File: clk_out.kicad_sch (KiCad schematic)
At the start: 14 parts

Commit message: Schematic updated
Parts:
- C701, C702, C703: renamed from C?; footprint (none) -> Capacitor_SMD:C_0805_2012Metric
- R701, R702: renamed from R?; footprint (none) -> Resistor_SMD:R_0805_2012Metric
- gave numbers to parts that had none: 6
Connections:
- net +3.3VA renamed +3.3VD
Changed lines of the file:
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@@
   (symbol (lib_id "symbols:74LVC1G157") (at 139.7 57.15 0) (unit 2)
     (in_bom yes) (on_board yes) (fields_autoplaced)
-    (property "Reference" "U?" (id 0) (at 137.4787 56.2415 0)
+    (property "Reference" "U701" (id 0) (at 137.4787 56.2415 0)
       (effects (font (size 1.27 1.27)) (justify right))
     )
@@
   (symbol (lib_id "Device:R") (at 184.15 101.6 270) (unit 1)
     (in_bom yes) (on_board yes) (fields_autoplaced)
-    (property "Reference" "R?" (id 0) (at 184.15 96.6175 90))
+    (property "Reference" "R701" (id 0) (at 184.15 96.6175 90))
     (property "Value" "75" (id 1) (at 184.15 99.3926 90))
-    (property "Footprint" "" (id 2) (at 184.15 99.822 90)
+    (property "Footprint" "Resistor_SMD:R_0805_2012Metric" (id 2) (at 184.15 99.822 90)
       (effects (font (size 1.27 1.27)) hide)
     )
@@
   (symbol (lib_id "power:GND") (at 190.5 113.03 0) (unit 1)
     (in_bom yes) (on_board yes) (fields_autoplaced)
-    (property "Reference" "#PWR?" (id 0) (at 190.5 119.38 0)
+    (property "Reference" "#PWR0705" (id 0) (at 190.5 119.38 0)
       (effects (font (size 1.27 1.27)) hide)
     )
@@
   (symbol (lib_id "Device:C") (at 171.45 101.6 90) (unit 1)
     (in_bom yes) (on_board yes) (fields_autoplaced)
-    (property "Reference" "C?" (id 0) (at 171.45 95.4745 90))
+    (property "Reference" "C702" (id 0) (at 171.45 95.4745 90))
     (property "Value" "100n" (id 1) (at 171.45 98.2496 90))
-    (property "Footprint" "" (id 2) (at 175.26 100.6348 0)
+    (property "Footprint" "Capacitor_SMD:C_0805_2012Metric" (id 2) (at 175.26 100.6348 0)
       (effects (font (size 1.27 1.27)) hide)
     )
@@
     (pin "2")
   )
-  (symbol (lib_id "symbols:+3.3VD") (at 152.4 90.17 0) (unit 1)
-    (in_bom yes) (on_board yes) (fields_autoplaced)
-    (property "Reference" "#PWR?" (id 0) (at 152.4 93.98 0)
+  (symbol (lib_name "+3.3VD_1") (lib_id "symbols:+3.3VD") (at 152.4 90.17 0) (unit 1)
+    (in_bom yes) (on_board yes) (fields_autoplaced)
+    (property "Reference" "#PWR0703" (id 0) (at 152.4 93.98 0)
       (effects (font (size 1.27 1.27)) hide)
     )
@@
   (symbol (lib_id "symbols:74LVC2G04") (at 128.27 93.98 0) (unit 1)
     (in_bom yes) (on_board yes)
-    (property "Reference" "U?" (id 0) (at 130.1115 84.9335 0))
+    (property "Reference" "U702" (id 0) (at 130.1115 84.9335 0))
     (property "Value" "74LVC2G04" (id 1) (at 130.1115 87.7086 0))
     (property "Footprint" "Package_TO_SOT_SMD:SOT-23-6" (id 2) (at 128.27 76.2 0)
@@
   (symbol (lib_id "Diode:BAT54J") (at 152.4 107.95 270) (unit 1)
     (in_bom yes) (on_board yes) (fields_autoplaced)
-    (property "Reference" "D?" (id 0) (at 154.432 106.724 90)
+    (property "Reference" "D702" (id 0) (at 154.432 106.724 90)
       (effects (font (size 1.27 1.27)) (justify left))
     )
@@
   (symbol (lib_id "Jumper:Jumper_2_Open") (at 171.45 90.17 0) (unit 1)
     (in_bom yes) (on_board yes) (fields_autoplaced)
-    (property "Reference" "JP?" (id 0) (at 171.45 84.5525 0))
+    (property "Reference" "JP701" (id 0) (at 171.45 84.5525 0))
     (property "Value" "DC" (id 1) (at 171.45 87.3276 0))
     (property "Footprint" "" (id 2) (at 171.45 90.17 0)
@@
   (symbol (lib_id "Device:R") (at 190.5 107.95 180) (unit 1)
     (in_bom yes) (on_board yes) (fields_autoplaced)
-    (property "Reference" "R?" (id 0) (at 188.722 107.0415 0)
+    (property "Reference" "R702" (id 0) (at 188.722 107.0415 0)
       (effects (font (size 1.27 1.27)) (justify left))
     )
@@
       (effects (font (size 1.27 1.27)) (justify left))
     )
-    (property "Footprint" "" (id 2) (at 192.278 107.95 90)
+    (property "Footprint" "Resistor_SMD:R_0805_2012Metric" (id 2) (at 192.278 107.95 90)
       (effects (font (size 1.27 1.27)) hide)
     )
@@
   (symbol (lib_id "power:GND") (at 152.4 113.03 0) (unit 1)
     (in_bom yes) (on_board yes) (fields_autoplaced)
-    (property "Reference" "#PWR?" (id 0) (at 152.4 119.38 0)
+    (property "Reference" "#PWR0704" (id 0) (at 152.4 119.38 0)
       (effects (font (size 1.27 1.27)) hide)
     )
@@
   (symbol (lib_id "symbols:+3.3VD") (at 139.7 50.8 0) (unit 1)
     (in_bom yes) (on_board yes) (fields_autoplaced)
-    (property "Reference" "#PWR?" (id 0) (at 139.7 54.61 0)
+    (property "Reference" "#PWR0701" (id 0) (at 139.7 54.61 0)
       (effects (font (size 1.27 1.27)) hide)
     )
@@
   (symbol (lib_id "power:GND") (at 139.7 63.5 0) (unit 1)
     (in_bom yes) (on_board yes) (fields_autoplaced)
-    (property "Reference" "#PWR?" (id 0) (at 139.7 69.85 0)
+    (property "Reference" "#PWR0702" (id 0) (at 139.7 69.85 0)
       (effects (font (size 1.27 1.27)) hide)
     )
@@
   (symbol (lib_id "power:GND") (at 203.2 113.03 0) (unit 1)
     (in_bom yes) (on_board yes) (fields_autoplaced)
-    (property "Reference" "#PWR?" (id 0) (at 203.2 119.38 0)
+    (property "Reference" "#PWR0706" (id 0) (at 203.2 119.38 0)
       (effects (font (size 1.27 1.27)) hide)
     )
@@
   (symbol (lib_id "Diode:BAT54J") (at 152.4 95.25 270) (unit 1)
     (in_bom yes) (on_board yes) (fields_autoplaced)
-    (property "Reference" "D?" (id 0) (at 154.432 94.024 90)
+    (property "Reference" "D701" (id 0) (at 154.432 94.024 90)
       (effects (font (size 1.27 1.27)) (justify left))
     )
@@
   (symbol (lib_id "Device:C") (at 177.8 57.15 180) (unit 1)
     (in_bom yes) (on_board yes) (fields_autoplaced)
-    (property "Reference" "C?" (id 0) (at 180.721 56.2415 0)
+    (property "Reference" "C703" (id 0) (at 180.721 56.2415 0)
       (effects (font (size 1.27 1.27)) (justify right))
     )
@@
       (effects (font (size 1.27 1.27)) (justify right))
     )
-    (property "Footprint" "" (id 2) (at 176.8348 53.34 0)
+    (property "Footprint" "Capacitor_SMD:C_0805_2012Metric" (id 2) (at 176.8348 53.34 0)
       (effects (font (size 1.27 1.27)) hide)
     )
@@
   (symbol (lib_id "Device:D_TVS") (at 203.2 107.95 90) (unit 1)
     (in_bom yes) (on_board yes) (fields_autoplaced)
-    (property "Reference" "D?" (id 0) (at 201.1681 107.0415 90)
+    (property "Reference" "D703" (id 0) (at 201.1681 107.0415 90)
       (effects (font (size 1.27 1.27)) (justify left))
     )
@@
   (symbol (lib_id "symbols:74LVC2G04") (at 152.4 57.15 0) (unit 3)
     (in_bom yes) (on_board yes)
-    (property "Reference" "U?" (id 0) (at 151.13 48.26 0)
+    (property "Reference" "U702" (id 0) (at 151.13 48.26 0)
       (effects (font (size 1.27 1.27)) (justify left))
     )
@@
     (pin "5")
   )
-  (symbol (lib_name "74LVC1G157_1") (lib_id "symbols:74LVC1G157") (at 104.14 101.6 0) (unit 1)
-    (in_bom yes) (on_board yes) (fields_autoplaced)
-    (property "Reference" "U?" (id 0) (at 104.14 90.7755 0))
+  (symbol (lib_id "symbols:74LVC1G157") (at 104.14 101.6 0) (unit 1)
+    (in_bom yes) (on_board yes) (fields_autoplaced)
+    (property "Reference" "U701" (id 0) (at 104.14 90.7755 0))
     (property "Value" "74LVC1G157" (id 1) (at 104.14 93.5506 0))
     (property "Footprint" "Package_TO_SOT_SMD:SOT-23-6" (id 2) (at 104.14 92.075 0)
@@
   (symbol (lib_id "Device:C") (at 165.1 57.15 180) (unit 1)
     (in_bom yes) (on_board yes) (fields_autoplaced)
-    (property "Reference" "C?" (id 0) (at 168.021 56.2415 0)
+    (property "Reference" "C701" (id 0) (at 168.021 56.2415 0)
       (effects (font (size 1.27 1.27)) (justify right))
     )
@@
       (effects (font (size 1.27 1.27)) (justify right))
     )
-    (property "Footprint" "" (id 2) (at 164.1348 53.34 0)
+    (property "Footprint" "Capacitor_SMD:C_0805_2012Metric" (id 2) (at 164.1348 53.34 0)
       (effects (font (size 1.27 1.27)) hide)
     )
@@
   (symbol (lib_id "symbols:74LVC2G04") (at 128.27 109.22 0) (unit 2)
     (in_bom yes) (on_board yes) (fields_autoplaced)
-    (property "Reference" "U?" (id 0) (at 130.1115 101.4435 0))
+    (property "Reference" "U702" (id 0) (at 130.1115 101.4435 0))
     (property "Value" "74LVC2G04" (id 1) (at 130.1115 104.2186 0))
     (property "Footprint" "Package_TO_SOT_SMD:SOT-23-6" (id 2) (at 128.27 91.44 0)

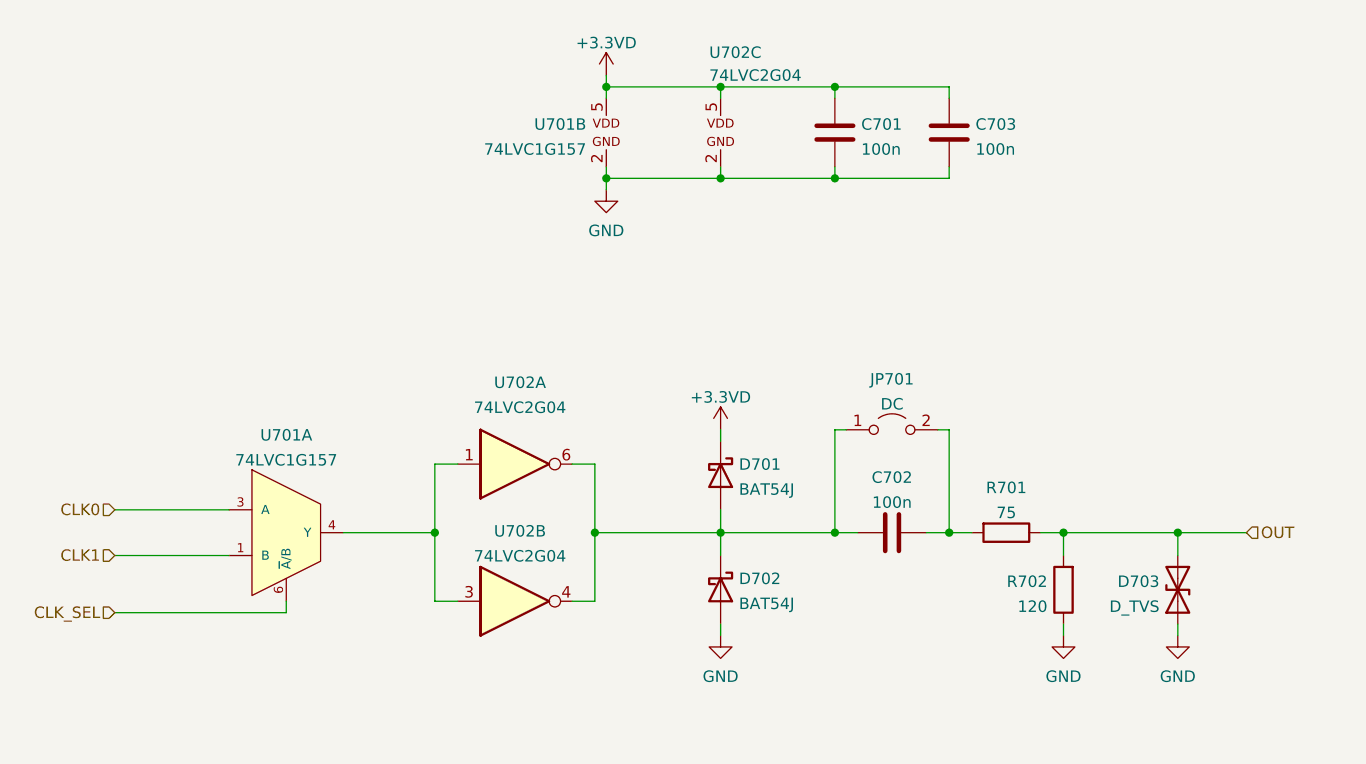
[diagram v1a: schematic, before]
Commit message: Schematic sketching done
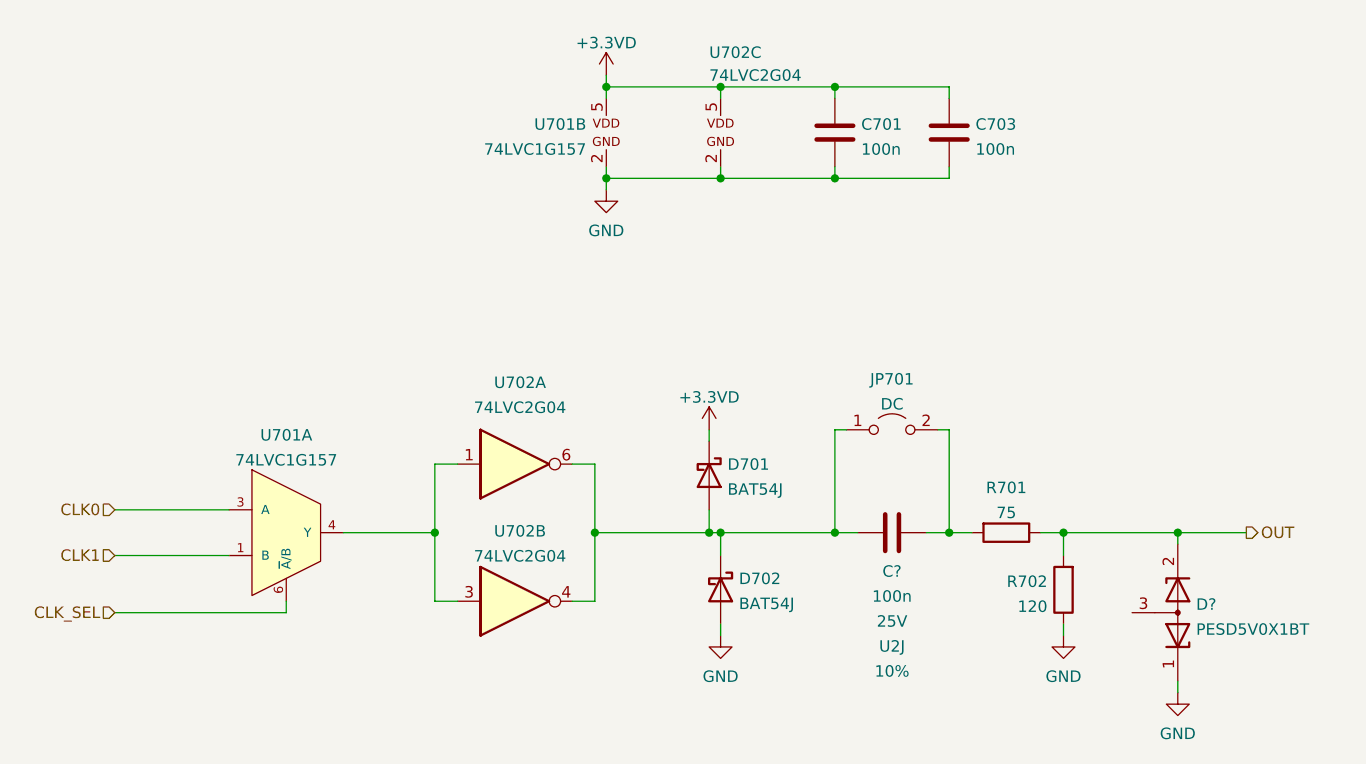
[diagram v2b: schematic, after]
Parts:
- removed C702: 100n, Capacitor_SMD:C_0805_2012Metric, symbol Device:C
- removed D703: D_TVS, symbol Device:D_TVS
- added C?: 100n, Capacitor_SMD:C_0805_2012Metric, symbol Device:C
- added D?: PESD5V0X1BT, Package_TO_SOT_SMD:SOT-23, symbol Device:D_Zener_Dual_CommonAnode_KKA
- R701, R702: Tolerance (none) -> 5%
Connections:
- net GND: now also D?.1 (K)
- net OUT: now also D?.2 (K)
- net at JP701.2 (B), R701.2: now also C?.2
- net at D701.2 (A), D702.1 (K), JP701.1 (A)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: now also C?.1
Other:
- moved on the sheet: D701

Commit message: Update schematic layout, separate into sheets
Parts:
- gave numbers to parts that had none: 2
- renumbered C701 to C1001, C703 to C1003, D701 to D1001, D702 to D1002, JP701 to JP1001, R701 to R1001, R702 to R1002, U701 to U1001, U702 to U1002
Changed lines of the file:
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@@
   (symbol (lib_id "symbols:74LVC1G157") (at 139.7 57.15 0) (unit 2)
     (in_bom yes) (on_board yes) (fields_autoplaced)
-    (property "Reference" "U701" (id 0) (at 137.4787 56.2415 0)
+    (property "Reference" "U1001" (id 0) (at 137.4787 56.2415 0)
       (effects (font (size 1.27 1.27)) (justify right))
     )
@@
   (symbol (lib_id "Device:R") (at 184.15 101.6 270) (unit 1)
     (in_bom yes) (on_board yes) (fields_autoplaced)
-    (property "Reference" "R701" (id 0) (at 184.15 96.6175 90))
+    (property "Reference" "R1001" (id 0) (at 184.15 96.6175 90))
     (property "Value" "75" (id 1) (at 184.15 99.3926 90))
     (property "Footprint" "Resistor_SMD:R_0805_2012Metric" (id 2) (at 184.15 99.822 90)
@@
   (symbol (lib_id "power:GND") (at 203.2 119.38 0) (unit 1)
     (in_bom yes) (on_board yes) (fields_autoplaced)
-    (property "Reference" "#PWR?" (id 0) (at 203.2 125.73 0)
+    (property "Reference" "#PWR01006" (id 0) (at 203.2 125.73 0)
       (effects (font (size 1.27 1.27)) hide)
     )
@@
   (symbol (lib_id "power:GND") (at 190.5 113.03 0) (unit 1)
     (in_bom yes) (on_board yes) (fields_autoplaced)
-    (property "Reference" "#PWR0705" (id 0) (at 190.5 119.38 0)
+    (property "Reference" "#PWR01005" (id 0) (at 190.5 119.38 0)
       (effects (font (size 1.27 1.27)) hide)
     )
@@
   (symbol (lib_id "Device:C") (at 171.45 101.6 90) (unit 1)
     (in_bom yes) (on_board yes) (fields_autoplaced)
-    (property "Reference" "C?" (id 0) (at 171.45 105.9085 90))
+    (property "Reference" "C1002" (id 0) (at 171.45 105.9085 90))
     (property "Value" "100n" (id 1) (at 171.45 108.6836 90))
     (property "Footprint" "Capacitor_SMD:C_0805_2012Metric" (id 2) (at 175.26 100.6348 0)
@@
     (pin "2")
   )
-  (symbol (lib_name "+3.3VD_1") (lib_id "symbols:+3.3VD") (at 151.13 90.17 0) (unit 1)
-    (in_bom yes) (on_board yes) (fields_autoplaced)
-    (property "Reference" "#PWR0703" (id 0) (at 151.13 93.98 0)
+  (symbol (lib_id "symbols:+3.3VD") (at 151.13 90.17 0) (unit 1)
+    (in_bom yes) (on_board yes) (fields_autoplaced)
+    (property "Reference" "#PWR01003" (id 0) (at 151.13 93.98 0)
       (effects (font (size 1.27 1.27)) hide)
     )
@@
   (symbol (lib_id "symbols:74LVC2G04") (at 128.27 93.98 0) (unit 1)
     (in_bom yes) (on_board yes)
-    (property "Reference" "U702" (id 0) (at 130.1115 84.9335 0))
+    (property "Reference" "U1002" (id 0) (at 130.1115 84.9335 0))
     (property "Value" "74LVC2G04" (id 1) (at 130.1115 87.7086 0))
     (property "Footprint" "Package_TO_SOT_SMD:SOT-23-6" (id 2) (at 128.27 76.2 0)
@@
   (symbol (lib_id "Diode:BAT54J") (at 152.4 107.95 270) (unit 1)
     (in_bom yes) (on_board yes) (fields_autoplaced)
-    (property "Reference" "D702" (id 0) (at 154.432 106.724 90)
+    (property "Reference" "D1002" (id 0) (at 154.432 106.724 90)
       (effects (font (size 1.27 1.27)) (justify left))
     )
@@
   (symbol (lib_id "Device:D_Zener_Dual_CommonAnode_KKA") (at 203.2 110.49 270) (mirror x) (unit 1)
     (in_bom yes) (on_board yes) (fields_autoplaced)
-    (property "Reference" "D?" (id 0) (at 205.232 109.5815 90)
+    (property "Reference" "D1003" (id 0) (at 205.232 109.5815 90)
       (effects (font (size 1.27 1.27)) (justify left))
     )
@@
   (symbol (lib_id "Jumper:Jumper_2_Open") (at 171.45 90.17 0) (unit 1)
     (in_bom yes) (on_board yes) (fields_autoplaced)
-    (property "Reference" "JP701" (id 0) (at 171.45 84.5525 0))
+    (property "Reference" "JP1001" (id 0) (at 171.45 84.5525 0))
     (property "Value" "DC" (id 1) (at 171.45 87.3276 0))
     (property "Footprint" "" (id 2) (at 171.45 90.17 0)
@@
   (symbol (lib_id "Device:R") (at 190.5 107.95 180) (unit 1)
     (in_bom yes) (on_board yes) (fields_autoplaced)
-    (property "Reference" "R702" (id 0) (at 188.722 107.0415 0)
+    (property "Reference" "R1002" (id 0) (at 188.722 107.0415 0)
       (effects (font (size 1.27 1.27)) (justify left))
     )
@@
   (symbol (lib_id "power:GND") (at 152.4 113.03 0) (unit 1)
     (in_bom yes) (on_board yes) (fields_autoplaced)
-    (property "Reference" "#PWR0704" (id 0) (at 152.4 119.38 0)
+    (property "Reference" "#PWR01004" (id 0) (at 152.4 119.38 0)
       (effects (font (size 1.27 1.27)) hide)
     )
@@
   (symbol (lib_id "symbols:+3.3VD") (at 139.7 50.8 0) (unit 1)
     (in_bom yes) (on_board yes) (fields_autoplaced)
-    (property "Reference" "#PWR0701" (id 0) (at 139.7 54.61 0)
+    (property "Reference" "#PWR01001" (id 0) (at 139.7 54.61 0)
       (effects (font (size 1.27 1.27)) hide)
     )
@@
   (symbol (lib_id "power:GND") (at 139.7 63.5 0) (unit 1)
     (in_bom yes) (on_board yes) (fields_autoplaced)
-    (property "Reference" "#PWR0702" (id 0) (at 139.7 69.85 0)
+    (property "Reference" "#PWR01002" (id 0) (at 139.7 69.85 0)
       (effects (font (size 1.27 1.27)) hide)
     )
@@
   (symbol (lib_id "Diode:BAT54J") (at 151.13 95.25 270) (unit 1)
     (in_bom yes) (on_board yes) (fields_autoplaced)
-    (property "Reference" "D701" (id 0) (at 153.162 94.024 90)
+    (property "Reference" "D1001" (id 0) (at 153.162 94.024 90)
       (effects (font (size 1.27 1.27)) (justify left))
     )
@@
   (symbol (lib_id "Device:C") (at 177.8 57.15 180) (unit 1)
     (in_bom yes) (on_board yes) (fields_autoplaced)
-    (property "Reference" "C703" (id 0) (at 180.721 56.2415 0)
+    (property "Reference" "C1003" (id 0) (at 180.721 56.2415 0)
       (effects (font (size 1.27 1.27)) (justify right))
     )
@@
   (symbol (lib_id "symbols:74LVC2G04") (at 152.4 57.15 0) (unit 3)
     (in_bom yes) (on_board yes)
-    (property "Reference" "U702" (id 0) (at 151.13 48.26 0)
+    (property "Reference" "U1002" (id 0) (at 151.13 48.26 0)
       (effects (font (size 1.27 1.27)) (justify left))
     )
@@
   (symbol (lib_id "symbols:74LVC1G157") (at 104.14 101.6 0) (unit 1)
     (in_bom yes) (on_board yes) (fields_autoplaced)
-    (property "Reference" "U701" (id 0) (at 104.14 90.7755 0))
+    (property "Reference" "U1001" (id 0) (at 104.14 90.7755 0))
     (property "Value" "74LVC1G157" (id 1) (at 104.14 93.5506 0))
     (property "Footprint" "Package_TO_SOT_SMD:SOT-23-6" (id 2) (at 104.14 92.075 0)
@@
   (symbol (lib_id "Device:C") (at 165.1 57.15 180) (unit 1)
     (in_bom yes) (on_board yes) (fields_autoplaced)
-    (property "Reference" "C701" (id 0) (at 168.021 56.2415 0)
+    (property "Reference" "C1001" (id 0) (at 168.021 56.2415 0)
       (effects (font (size 1.27 1.27)) (justify right))
     )
@@
   (symbol (lib_id "symbols:74LVC2G04") (at 128.27 109.22 0) (unit 2)
     (in_bom yes) (on_board yes) (fields_autoplaced)
-    (property "Reference" "U702" (id 0) (at 130.1115 101.4435 0))
+    (property "Reference" "U1002" (id 0) (at 130.1115 101.4435 0))
     (property "Value" "74LVC2G04" (id 1) (at 130.1115 104.2186 0))
     (property "Footprint" "Package_TO_SOT_SMD:SOT-23-6" (id 2) (at 128.27 91.44 0)

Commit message: Schematic update
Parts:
- C1001: value 100n -> 1u; Spec1 (none) -> 16V; Spec2 (none) -> X5R; Tolerance (none) -> 20%
- C1002: footprint Capacitor_SMD:C_0805_2012Metric -> Capacitor_SMD:C_1206_3216Metric
- C1003: Spec1 (none) -> 16V; Spec2 (none) -> X5R; Tolerance (none) -> 20%
- JP1001: footprint (none) -> Connector_PinHeader_2.54mm:PinHeader_1x02_P2.54mm_Vertical
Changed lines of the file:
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@@
     (property "Reference" "C1002" (id 0) (at 171.45 105.9085 90))
     (property "Value" "100n" (id 1) (at 171.45 108.6836 90))
-    (property "Footprint" "Capacitor_SMD:C_0805_2012Metric" (id 2) (at 175.26 100.6348 0)
+    (property "Footprint" "Capacitor_SMD:C_1206_3216Metric" (id 2) (at 175.26 100.6348 0)
       (effects (font (size 1.27 1.27)) hide)
     )
@@
     (property "Reference" "JP1001" (id 0) (at 171.45 84.5525 0))
     (property "Value" "DC" (id 1) (at 171.45 87.3276 0))
-    (property "Footprint" "" (id 2) (at 171.45 90.17 0)
+    (property "Footprint" "Connector_PinHeader_2.54mm:PinHeader_1x02_P2.54mm_Vertical" (id 2) (at 171.45 90.17 0)
       (effects (font (size 1.27 1.27)) hide)
     )
@@
     )
     (property "Datasheet" "~" (id 3) (at 177.8 57.15 0)
+      (effects (font (size 1.27 1.27)) hide)
+    )
+    (property "Spec1" "16V" (id 4) (at 177.8 57.15 0)
+      (effects (font (size 1.27 1.27)) hide)
+    )
+    (property "Spec2" "X5R" (id 5) (at 177.8 57.15 0)
+      (effects (font (size 1.27 1.27)) hide)
+    )
+    (property "Tolerance" "20%" (id 6) (at 177.8 57.15 0)
       (effects (font (size 1.27 1.27)) hide)
     )
@@
       (effects (font (size 1.27 1.27)) (justify right))
     )
-    (property "Value" "100n" (id 1) (at 168.021 59.0166 0)
+    (property "Value" "1u" (id 1) (at 168.021 59.0166 0)
       (effects (font (size 1.27 1.27)) (justify right))
     )
@@
       (effects (font (size 1.27 1.27)) hide)
     )
+    (property "Spec1" "16V" (id 4) (at 165.1 57.15 0)
+      (effects (font (size 1.27 1.27)) hide)
+    )
+    (property "Spec2" "X5R" (id 5) (at 165.1 57.15 0)
+      (effects (font (size 1.27 1.27)) hide)
+    )
+    (property "Tolerance" "20%" (id 6) (at 165.1 57.15 0)
+      (effects (font (size 1.27 1.27)) hide)
+    )
